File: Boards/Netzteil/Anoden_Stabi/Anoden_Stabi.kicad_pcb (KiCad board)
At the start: 2 copper layers, 100 x 80 mm, 27 parts, among them J1 Conn_01x06, P1 CONN_3, Q1 2SC2979, Q2 MJE5731

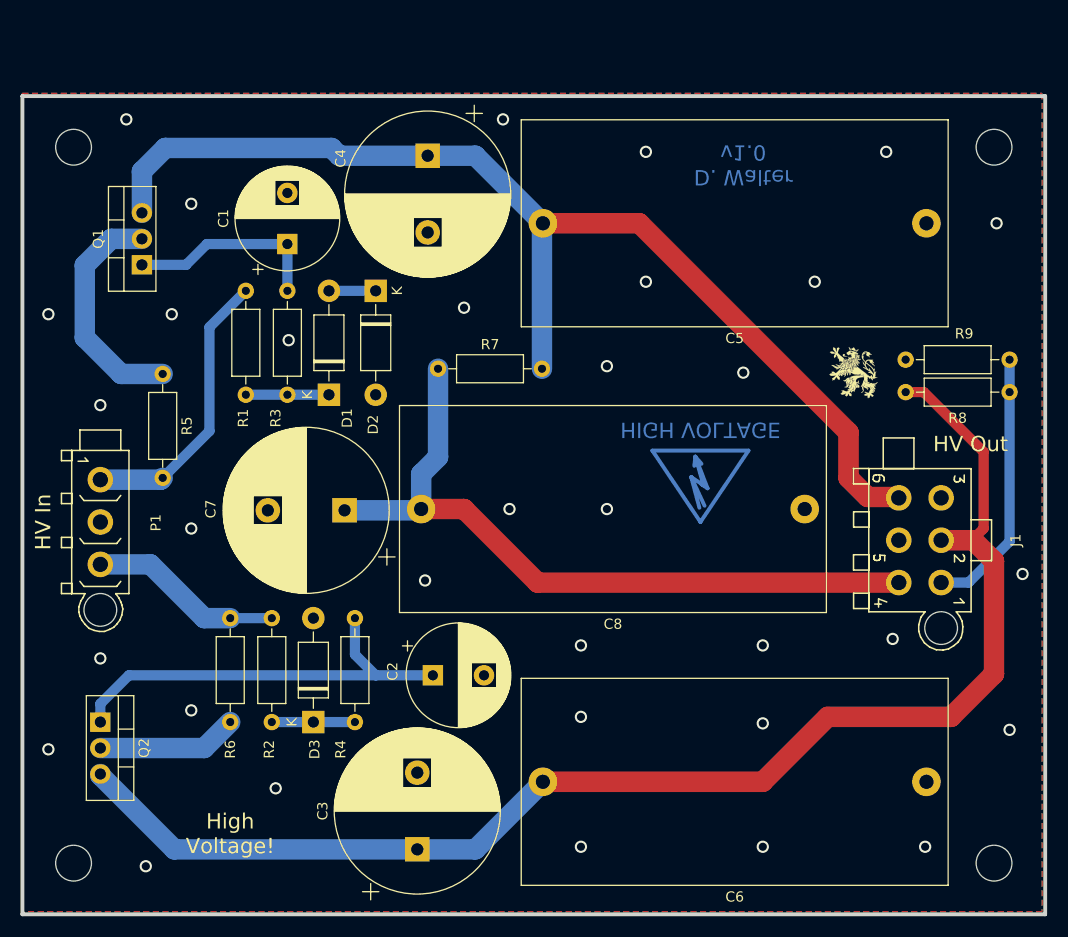
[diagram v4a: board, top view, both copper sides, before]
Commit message: Reworked Delay + Layout changed
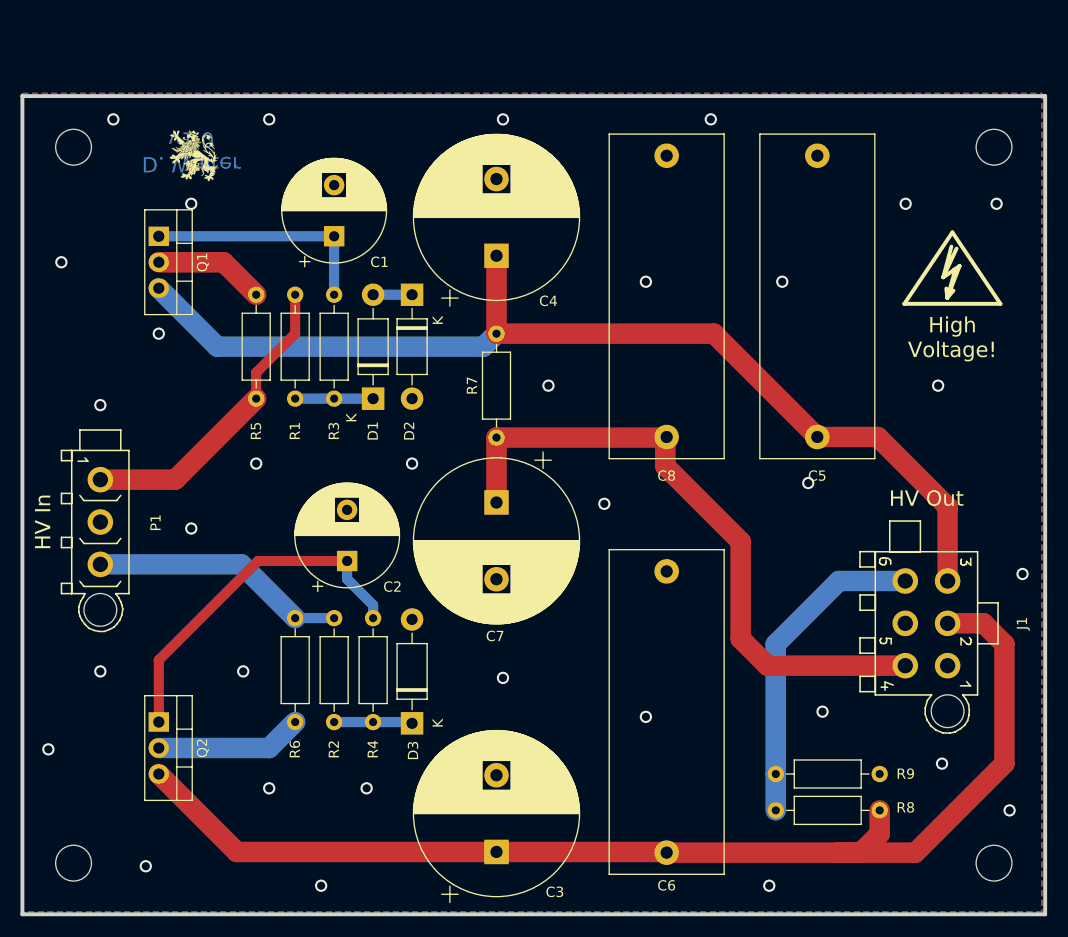
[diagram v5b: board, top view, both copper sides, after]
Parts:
- removed the REF** at (142.5, 86.0)
- added REF**: Symbol_HighVoltage_Type2_SilkTop_VerySmall, Loewe:Symbol_HighVoltage_Type2_SilkTop_VerySmall, F.Cu at (167.1, 66.0)
- C5, C6, C8: footprint Capacitor_THT:C_Rect_L41.5mm_W20.0mm_P37.50mm_MKS4 -> Capacitor_THT:C_Rect_L31.5mm_W11.0mm_P27.50mm_MKS4
- moved G*** 67.9 mm to (93.0, 54.4)
- moved R8 46.8 mm to (149.9, 118.4), turned to 0 degrees
- moved R9 40.6 mm to (160.0, 114.8), turned to 180 degrees
- moved C8 37.1 mm to (139.2, 54.4), turned to 270 degrees
- moved C6 32.7 mm to (139.2, 95.0), turned to 270 degrees
- moved C7 14.9 mm to (122.6, 88.3), turned to 270 degrees
- moved C2 14.0 mm to (108.0, 94.0), turned to 90 degrees
- moved C5 12.5 mm to (153.9, 54.4), turned to 270 degrees
- moved R5 12.0 mm to (99.1, 67.9)
- moved C4 11.9 mm to (122.6, 64.1), turned to 90 degrees
- moved D3 9.65 mm to (114.3, 109.9)
- moved R7 8.83 mm to (122.6, 81.9), turned to 90 degrees
- moved J1 8.15 mm to (164.6, 100.1)
- moved C3 7.75 mm to (122.6, 122.4)
- moved R6 6.35 mm to (102.9, 109.7)
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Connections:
- J1 pad 1: -60V -> GND
- J1 pad 3: GND -> +300V
- J1 pad 6: +300V -> -60V
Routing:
- net -120V: track 136.9 -> 114.7 mm
- net Net-(Q1-Pad2): track 22.8 -> 10.8 mm
- net +240V: track 71.6 -> 63.0 mm
- net +300V: track 110.1 -> 101.9 mm
- net Net-(C2-Pad1): track 41.9 -> 35.1 mm
- net -180V: track 18.9 -> 25.0 mm
- net -60V: track 26.1 -> 31.5 mm
- net Net-(C1-Pad1): track 19.6 -> 22.9 mm
- net +450V: track 27.8 -> 30.3 mm
- net Net-(D1-Pad2): track 4.57 -> 3.81 mm
- net Net-(Q2-Pad2): track 13.8 -> 14.4 mm
- net Net-(D1-Pad1): track 8.13 -> 7.62 mm
- net GND: vias 34 -> 33
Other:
- board text removed: "HIGH VOLTAGE"

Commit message: Work in progess - many LAyour changes
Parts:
- moved G*** 73.6 mm to (150.5, 100.3)
- moved R7 0.64 mm to (122.6, 81.3)
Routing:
- net +300V: track 101.9 -> 127.0 mm
- net +240V: track 63.0 -> 66.0 mm
- net GND: vias 33 -> 36
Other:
- rule pad_to_mask_clearance: 0.2 -> 0

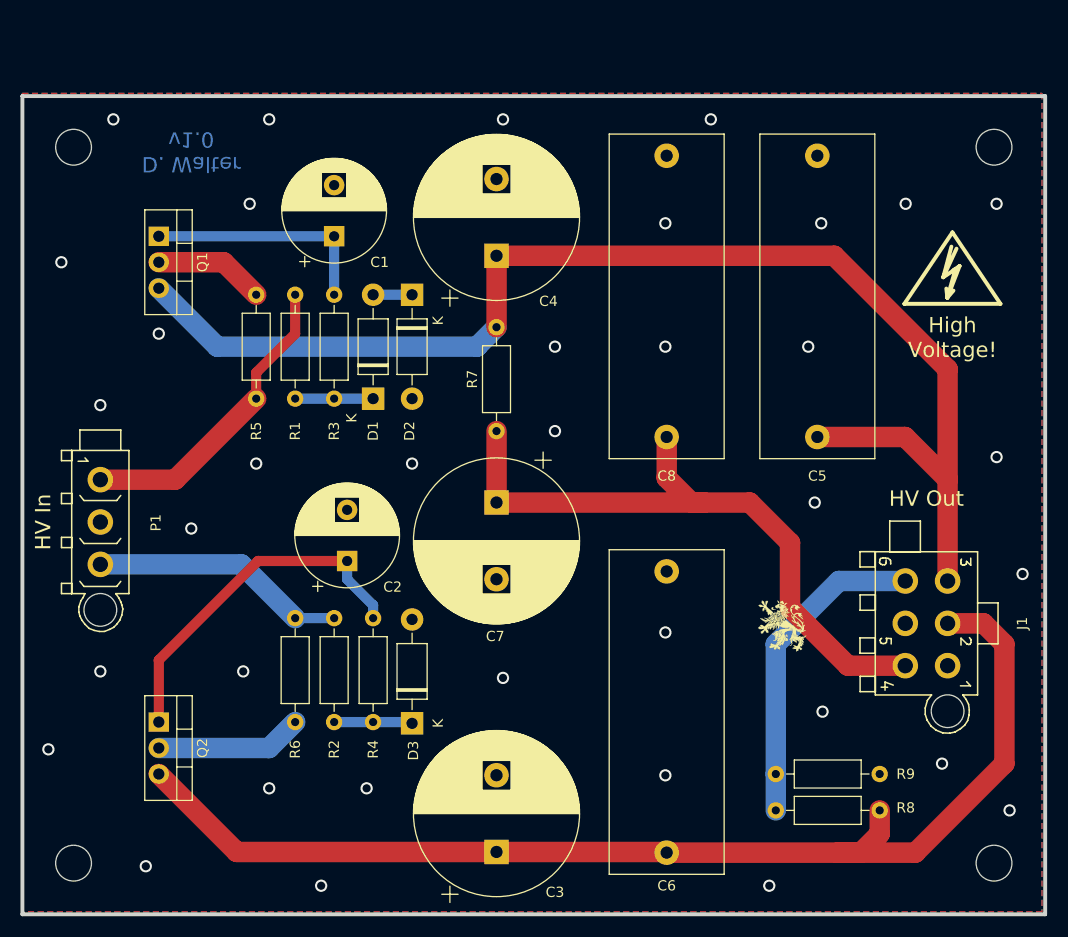
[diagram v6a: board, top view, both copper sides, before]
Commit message: 6.3V, 400V und 400V Regler Boards bestellt
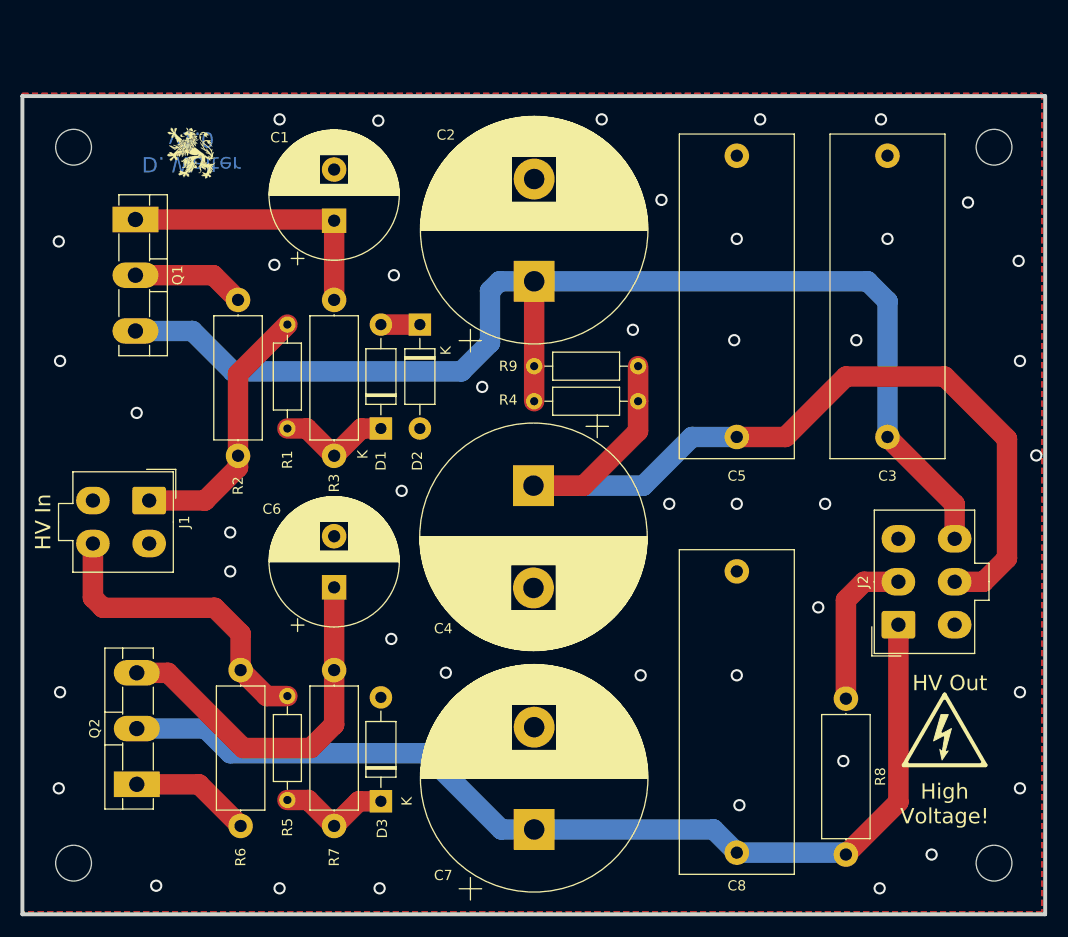
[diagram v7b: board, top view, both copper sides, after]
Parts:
- removed P1: CONN_3, Connectors_Mini-Universal:MiniUniversalMate-N-LokSocket_3PinVertical
- removed the REF** at (167.1, 66.0)
- added J1: Conn_01x04, Connector_Molex:Molex_Mini-Fit_Jr_5566-04A_2x02_P4.20mm_Vertical, F.Cu at (88.6, 88.1)
- added REF**: Symbol_HighVoltage_Triangle_8x7mm_Copper, Symbol:Symbol_HighVoltage_Triangle_8x7mm_Copper, F.Cu at (166.4, 110.5)
- C1: value 10µF/400V -> 10µF/450V; footprint Capacitor_THT:CP_Radial_D10.0mm_P5.00mm -> Capacitor_THT:CP_Radial_D12.5mm_P5.00mm
- C2: renamed from C4; footprint Capacitor_THT:CP_Radial_D16.0mm_P7.50mm -> Capacitor_THT:CP_Radial_D22.0mm_P10.00mm_SnapIn
- C4: renamed from C7; footprint Capacitor_THT:CP_Radial_D16.0mm_P7.50mm -> Capacitor_THT:CP_Radial_D22.0mm_P10.00mm_SnapIn
- C6: renamed from C2; value 10µF/400V -> 10µF/450V; footprint Capacitor_THT:CP_Radial_D10.0mm_P5.00mm -> Capacitor_THT:CP_Radial_D12.5mm_P5.00mm
- C7: renamed from C3; footprint Capacitor_THT:CP_Radial_D16.0mm_P7.50mm -> Capacitor_THT:CP_Radial_D22.0mm_P10.00mm_SnapIn
- J2: renamed from J1; footprint Connectors_Mini-Universal:MiniUniversalMate-N-LokSocket_6PinVertical -> Connector_Molex:Molex_Mini-Fit_Jr_5566-06A_2x03_P4.20mm_Vertical
- Q1: value 2SC2979 -> BU508A; footprint Package_TO_SOT_THT:TO-220-3_Vertical -> Package_TO_SOT_THT:TO-3P-3_Vertical
- Q2: value MJE5731 -> 2SA1943; footprint Package_TO_SOT_THT:TO-220-3_Vertical -> Package_TO_SOT_THT:TO-3P-3_Vertical
- R2: renamed from R5; footprint Resistor_THT:R_Axial_DIN0207_L6.3mm_D2.5mm_P10.16mm_Horizontal -> Resistor_THT:R_Axial_DIN0414_L11.9mm_D4.5mm_P15.24mm_Horizontal
- R3, R6, R8: footprint Resistor_THT:R_Axial_DIN0207_L6.3mm_D2.5mm_P10.16mm_Horizontal -> Resistor_THT:R_Axial_DIN0414_L11.9mm_D4.5mm_P15.24mm_Horizontal
- R7: renamed from R4; footprint Resistor_THT:R_Axial_DIN0207_L6.3mm_D2.5mm_P10.16mm_Horizontal -> Resistor_THT:R_Axial_DIN0414_L11.9mm_D4.5mm_P15.24mm_Horizontal
- R9: value 10k -> 30k
- moved G*** 74.0 mm to (92.7, 54.1)
- moved R9 46.3 mm to (136.4, 74.9)
- moved R4 14.1 mm to (136.4, 78.4), turned to 180 degrees
- moved R8 12.9 mm to (156.7, 107.4), turned to -90 degrees
- moved R6 11.5 mm to (97.5, 119.9)
- moved R7 10.9 mm to (106.7, 119.9)
- moved R5 8.89 mm to (102.1, 117.3)
- moved D3 8.21 mm to (111.3, 117.5)
- moved C3 6.86 mm to (160.8, 54.4)
- moved C5 6.86 mm to (146.1, 54.4)
- moved C8 6.86 mm to (146.1, 95.0)
- moved Q2 6.45 mm to (87.4, 115.8), turned to 90 degrees
- moved R3 5.59 mm to (106.7, 83.7)
- moved C2 4.45 mm to (126.2, 66.6)
- moved C7 4.29 mm to (126.2, 120.2)
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- renumbered C5 to C3, C8 to C5, C6 to C8, R7 to R4, R2 to R5
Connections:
- C6 pad 1: Net-(C2-Pad1) -> Net-(Q2-B)
- J2 pad 1: GND -> -120V
- J2 pad 2: -120V -> -60V
- J2 pad 3: +300V -> GND
- J2 pad 4: +240V -> GND
- J2 pad 5: GND -> +240V
- J2 pad 6: -60V -> +300V
- Q2 pad 1: Net-(C2-Pad1) -> Net-(Q2-E)
- Q2 pad 2: Net-(Q2-Pad2) -> -120V
- Q2 pad 3: -120V -> Net-(Q2-B)
- R6 pad 1: Net-(Q2-Pad2) -> Net-(Q2-E)
- R7 pad 2: Net-(C2-Pad1) -> Net-(Q2-B)
- R9 pad 1: GND -> +240V
- R9 pad 2: -60V -> +300V
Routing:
- net Net-(Q2-B): track 0.00 -> 36.7 mm
- net Net-(C2-Pad1): track 35.1 -> 0.00 mm
- net +240V: track 66.0 -> 89.8 mm
- net -60V: track 31.5 -> 15.5 mm
- net -120V: track 114.7 -> 99.0 mm
- net Net-(Q2-Pad2): track 14.4 -> 0.00 mm
- net Net-(Q2-E): track 0.00 -> 11.8 mm
- net +300V: track 127.0 -> 120.5 mm
- net -180V: track 25.0 -> 30.4 mm
- net Net-(Q1-B): track 22.9 -> 27.2 mm
- net +450V: track 30.3 -> 26.0 mm
- net Net-(D1-K): track 7.62 -> 11.4 mm
- net Net-(D3-K): track 7.85 -> 11.2 mm
- net GND: vias 36 -> 43
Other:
- net class Default removed

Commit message: Leiterplatte erstellt
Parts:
- removed G***: LOGO, Loewe:Loewe_Klein
- C2, C4, C7: footprint Capacitor_THT:CP_Radial_D22.0mm_P10.00mm_SnapIn -> Capacitor_THT:CP_Radial_D17.0mm_P7.50mm
